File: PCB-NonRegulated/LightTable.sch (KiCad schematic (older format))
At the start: 19 parts, among them CON1 BARREL_JACK, P1 CONN_2_V, P2 CONN_01X01, P3 CONN_01X01, P4 CONN_01X01, P5 CONN_01X01, P6 CONN_01X01, P7 CONN_01X01, P8 CONN_4_V, U1 MosfetIRF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

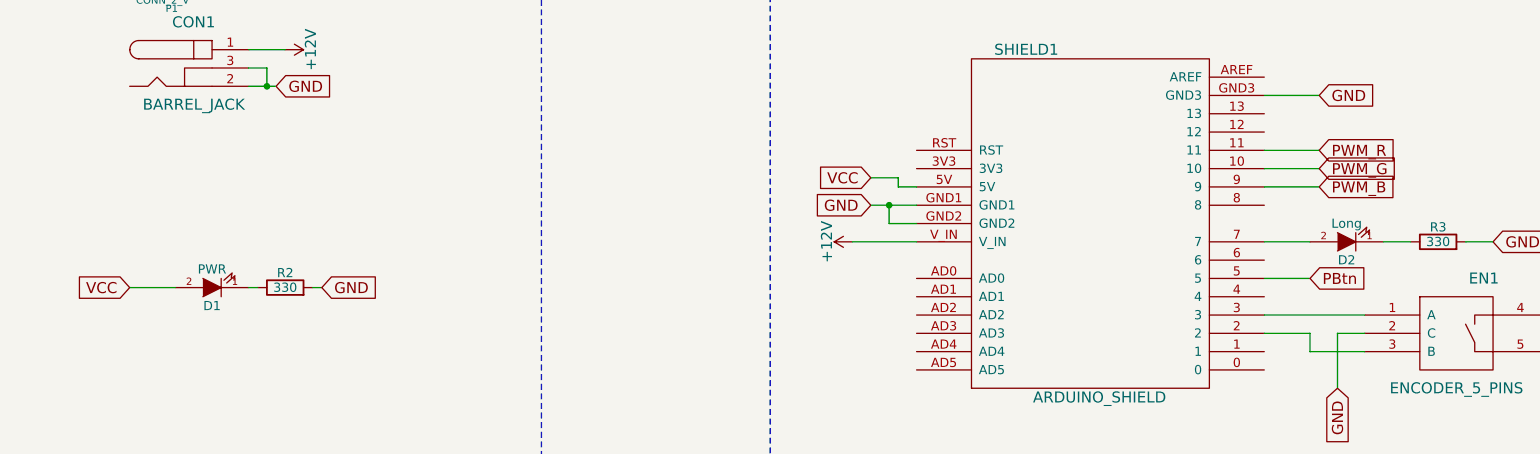
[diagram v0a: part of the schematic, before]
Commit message: Fixed wrong placement of shield and added gerbers
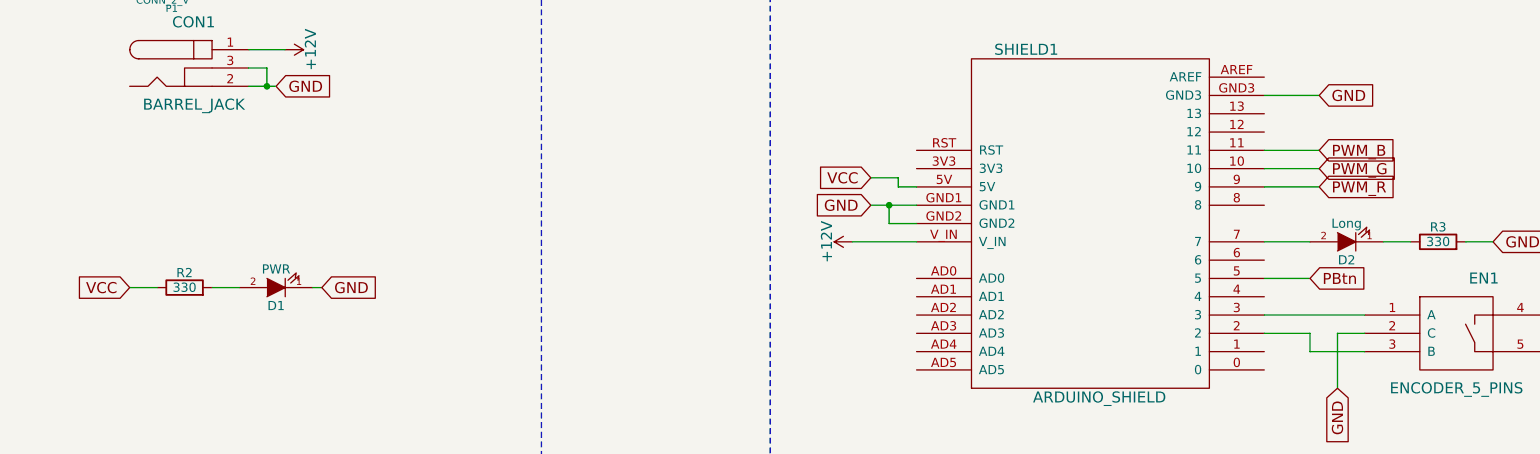
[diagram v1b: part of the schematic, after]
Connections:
- net GND: now also D1.1 (K); no longer R2.2
- net PWM_B: now also SHIELD1.11; no longer SHIELD1.9
- net PWM_R: now also SHIELD1.9; no longer SHIELD1.11
- net VCC: now also R2.1; no longer D1.2 (A)
- new net: D1.2 (A), R2.2
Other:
- moved on the sheet: D1, R2
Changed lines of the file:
@@
 Text GLabel 2400 5450 3    60   Input ~ 0
 R
-Text GLabel 8050 2000 2    60   Input ~ 0
+Text GLabel 8050 2200 2    60   Input ~ 0
 PWM_R
 Text GLabel 3800 5450 3    60   Input ~ 0
@@
 Text GLabel 8050 2100 2    60   Input ~ 0
 PWM_G
-Text GLabel 8050 2200 2    60   Input ~ 0
+Text GLabel 8050 2000 2    60   Input ~ 0
 PWM_B
 $Comp
@@
 	8850 2500 9000 2500
 Wire Wire Line
-	1550 2750 1800 2750
-Wire Wire Line
-	2250 2750 2200 2750
-Wire Wire Line
 	2600 2750 2550 2750
 Text GLabel 2600 2750 2    60   Input ~ 0
@@
 L R R2
 U 1 1 55CC852C
-P 2400 2750
-F 0 "R2" V 2480 2750 50  0000 C CNN
-F 1 "330" V 2400 2750 50  0000 C CNN
-F 2 "Resistors_ThroughHole:Resistor_Horizontal_RM10mm" V 2330 2750 30  0001 C CNN
-F 3 "" H 2400 2750 30  0000 C CNN
-	1    2400 2750
+P 1850 2750
+F 0 "R2" V 1930 2750 50  0000 C CNN
+F 1 "330" V 1850 2750 50  0000 C CNN
+F 2 "Resistors_ThroughHole:Resistor_Horizontal_RM10mm" V 1780 2750 30  0001 C CNN
+F 3 "" H 1850 2750 30  0000 C CNN
+	1    1850 2750
 	0    -1   -1   0
 $EndComp
@@
 L LED D1
 U 1 1 55CC841D
-P 2000 2750
-F 0 "D1" H 2000 2850 50  0000 C CNN
-F 1 "PWR" H 2000 2650 50  0000 C CNN
-F 2 "LEDs:LED-5MM" H 2000 2750 60  0001 C CNN
-F 3 "" H 2000 2750 60  0000 C CNN
-	1    2000 2750
+P 2350 2750
+F 0 "D1" H 2350 2850 50  0000 C CNN
+F 1 "PWR" H 2350 2650 50  0000 C CNN
+F 2 "LEDs:LED-5MM" H 2350 2750 60  0001 C CNN
+F 3 "" H 2350 2750 60  0000 C CNN
+	1    2350 2750
 	-1   0    0    1
 $EndComp
@@
 Wire Wire Line
 	5500 2500 5850 2500
+Wire Wire Line
+	1700 2750 1550 2750
+Wire Wire Line
+	2000 2750 2150 2750
 $EndSCHEMATC
